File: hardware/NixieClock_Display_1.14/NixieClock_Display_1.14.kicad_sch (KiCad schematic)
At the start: 2 parts, among them J1 Conn_01x08, J2 Conn_01x08

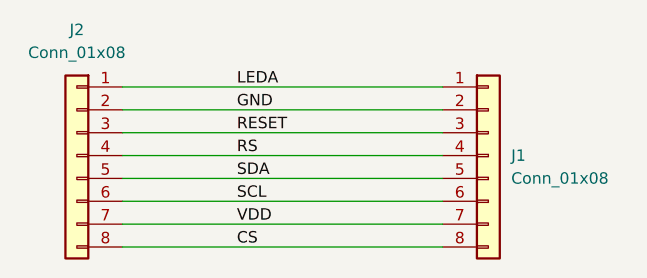
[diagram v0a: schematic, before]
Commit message: display 1.14 anpassungen. Stecker war verpolt
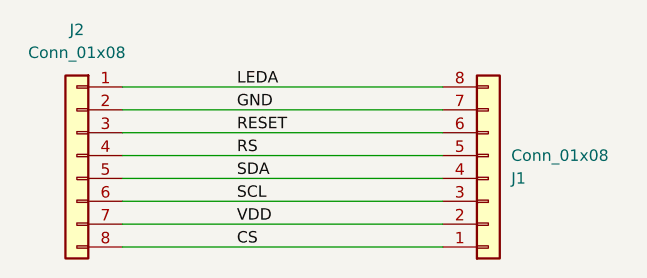
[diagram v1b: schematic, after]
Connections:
- net CS: now also J1.1 (Pin_1); no longer J1.8 (Pin_8)
- net GND: now also J1.7 (Pin_7); no longer J1.2 (Pin_2)
- net LEDA: now also J1.8 (Pin_8); no longer J1.1 (Pin_1)
- net RESET: now also J1.6 (Pin_6); no longer J1.3 (Pin_3)
- net RS: now also J1.5 (Pin_5); no longer J1.4 (Pin_4)
- net SCL: now also J1.3 (Pin_3); no longer J1.6 (Pin_6)
- net SDA: now also J1.4 (Pin_4); no longer J1.5 (Pin_5)
- net VDD: now also J1.2 (Pin_2); no longer J1.7 (Pin_7)
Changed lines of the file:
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@@
+	(wire
+		(pts
+			(xy 118.11 76.2) (xy 82.55 76.2)
+		)
+		(stroke
+			(width 0)
+			(type default)
+		)
+	)
+	(wire
+		(pts
+			(xy 118.11 68.58) (xy 82.55 68.58)
+		)
+		(stroke
+			(width 0)
+			(type default)
+		)
+	)
+	(wire
+		(pts
+			(xy 118.11 71.12) (xy 82.55 71.12)
+		)
+		(stroke
+			(width 0)
+			(type default)
+		)
+	)
+	(wire
+		(pts
+			(xy 118.11 81.28) (xy 82.55 81.28)
+		)
+		(stroke
+			(width 0)
+			(type default)
+		)
+	)
+	(wire
+		(pts
+			(xy 118.11 73.66) (xy 82.55 73.66)
+		)
+		(stroke
+			(width 0)
+			(type default)
+		)
+	)
+	(wire
+		(pts
+			(xy 118.11 78.74) (xy 82.55 78.74)
+		)
+		(stroke
+			(width 0)
+			(type default)
+		)
+	)
+	(wire
+		(pts
+			(xy 118.11 66.04) (xy 82.55 66.04)
+		)
+		(stroke
+			(width 0)
+			(type default)
+		)
+	)
 	(wire
 		(pts
 			(xy 118.11 83.82) (xy 82.55 83.82)
-		)
-		(stroke
-			(width 0)
-			(type default)
-		)
-	)
-	(wire
-		(pts
-			(xy 118.11 76.2) (xy 82.55 76.2)
-		)
-		(stroke
-			(width 0)
-			(type default)
-		)
-	)
-	(wire
-		(pts
-			(xy 118.11 78.74) (xy 82.55 78.74)
-		)
-		(stroke
-			(width 0)
-			(type default)
-		)
-	)
-	(wire
-		(pts
-			(xy 118.11 81.28) (xy 82.55 81.28)
-		)
-		(stroke
-			(width 0)
-			(type default)
-		)
-	)
-	(wire
-		(pts
-			(xy 118.11 68.58) (xy 82.55 68.58)
-		)
-		(stroke
-			(width 0)
-			(type default)
-		)
-	)
-	(wire
-		(pts
-			(xy 118.11 66.04) (xy 82.55 66.04)
-		)
-		(stroke
-			(width 0)
-			(type default)
-		)
-	)
-	(wire
-		(pts
-			(xy 118.11 73.66) (xy 82.55 73.66)
-		)
-		(stroke
-			(width 0)
-			(type default)
-		)
-	)
-	(wire
-		(pts
-			(xy 118.11 71.12) (xy 82.55 71.12)
 		)
 		(stroke
@@
 	(symbol
 		(lib_id "Connector_Generic:Conn_01x08")
-		(at 123.19 73.66 0)
+		(at 123.19 76.2 0)
+		(mirror x)
 		(unit 1)
 		(exclude_from_sim no)
@@
 		(on_board yes)
 		(dnp no)
-		(fields_autoplaced yes)
 		(property "Reference" "J1"
-			(at 125.73 73.6599 0)
+			(at 125.73 76.2001 0)
 			(effects
 				(font
@@
 		)
 		(property "Value" "Conn_01x08"
-			(at 125.73 76.1999 0)
+			(at 125.73 73.6601 0)
 			(effects
 				(font
@@
 		)
 		(property "Footprint" "Connector_FFC-FPC:Hirose_FH12-8S-0.5SH_1x08-1MP_P0.50mm_Horizontal"
-			(at 123.19 73.66 0)
+			(at 123.19 76.2 0)
 			(effects
 				(font
@@
 		)
 		(property "Datasheet" "~"
-			(at 123.19 73.66 0)
+			(at 123.19 76.2 0)
 			(effects
 				(font
@@
 		)
 		(property "Description" "Generic connector, single row, 01x08, script generated (kicad-library-utils/schlib/autogen/connector/)"
-			(at 123.19 73.66 0)
-			(effects
-				(font
+			(at 123.19 76.2 0)
+			(effects
+				(font
